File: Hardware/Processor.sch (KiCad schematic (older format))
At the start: 0 parts

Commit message: Add processor support circuitry
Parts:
- added C? (x2): C, ~, symbol C
- added C?: 10uF, ~, symbol C
- added C? (x2): 0.1uF, ~, symbol C
- added J?: ICSP-PIC, ~, symbol ICSP-PIC
- added J?: USB_MINI, ~, symbol USB_MINI
- added R? (x3): 10k, ~, symbol R
- added R?: R, ~, symbol R
- added SW?: PGM, ~, symbol SW-MOM
- added SW?: RST, ~, symbol SW-MOM
- added U?: PIC32MX250F128B, symbol PIC32MX250F128B
- added X?: 8MHz, ~, symbol CRYSTAL
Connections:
- net labels added: +3.3V, A1, A2, C, C1, C2, D+, D-, GND, ID, MCLR, OSC1, OSC2, PGC, PGD, PGM, VBus, VCap
- wire segments 0 -> 63
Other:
- note added: "A"

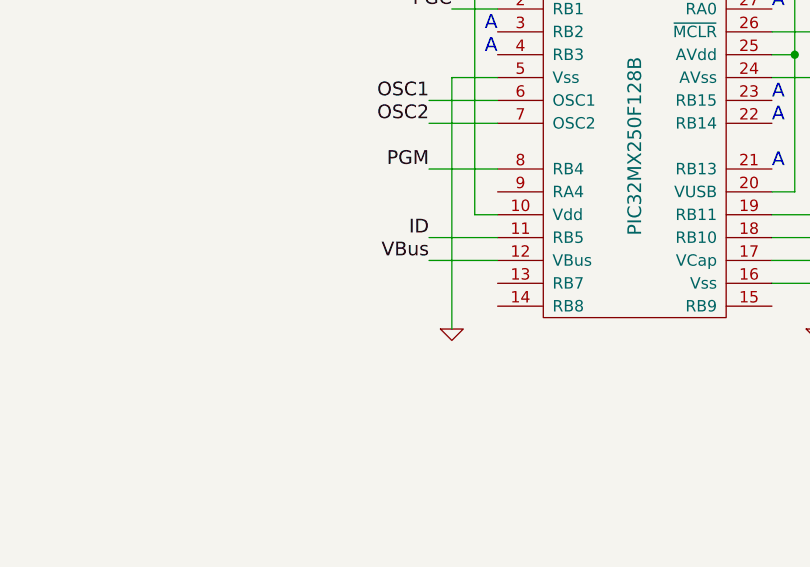
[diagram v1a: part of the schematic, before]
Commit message: Fill BOM fields of amplifier section
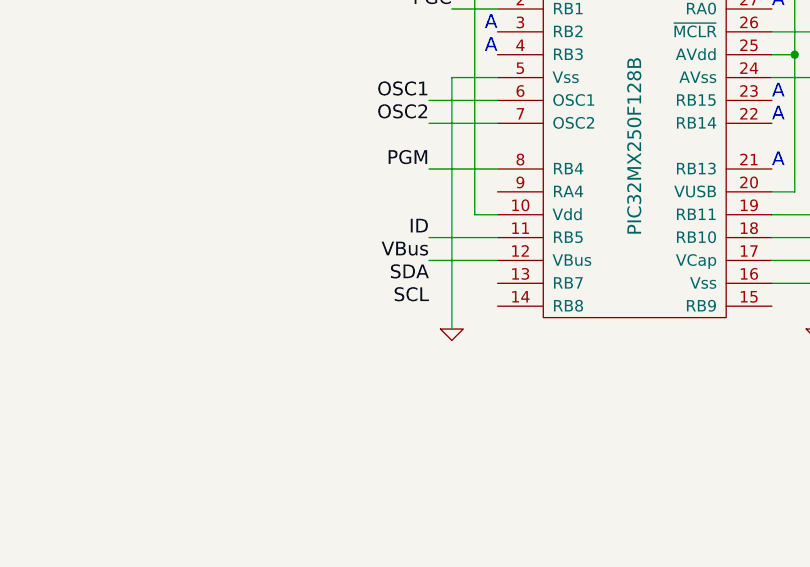
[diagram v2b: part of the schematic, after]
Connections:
- net labels added: SCL, SDA
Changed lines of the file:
@@
 Text Notes 5500 3700 2    60   ~ 0
 A
+Text Label 5200 4800 2    60   ~ 0
+SCL
+Text Label 5200 4700 2    60   ~ 0
+SDA
 $EndSCHEMATC

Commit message: Add second detection chain
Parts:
- removed C? (x2): 0.1uF, ~, symbol C
- removed R? (x2): 10k, ~, symbol R
- added C? (x2): 0.1uF, CAPC1608, symbol C
- added R? (x2): 10k, RESC1608, symbol R
- C?: footprint ~ -> CAPC2012; Dielectric D -> X5R; Distributor Part No (none) -> 1276-1052-1-ND; MFR Name (none) -> Samsung; MFR Part No (none) -> CL21A106KPFNNNE; Voltage V -> 10V
- R?: footprint ~ -> RESC1608; Distributor Part No (none) -> RMCF0603JT10K0CT-ND; MFR Name (none) -> Stackpole; MFR Part No (none) -> RMCF0603JT10K0; Power W -> 0.1W; Tolerance % -> 5%
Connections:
- wire segments 63 -> 72
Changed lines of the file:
@@
 $Descr A4 11693 8268
 encoding utf-8
-Sheet 5 5
+Sheet 5 7
 Title "Solid State Cosmic Ray Detector"
 Date "24 sep 2013"
@@
 $EndComp
 $Comp
-L R R?
-U 1 1 5240FDBF
-P 2600 2250
-F 0 "R?" H 2600 2350 50  0000 C CNN
-F 1 "10k" H 2600 2250 50  0000 C CNN
-F 2 "~" H 2600 2250 60  0000 C CNN
-F 3 "~" H 2600 2250 60  0000 C CNN
-F 4 "W" H 2600 2150 50  0001 C CNN "Power"
-F 5 "%" H 2600 2050 50  0001 C CNN "Tolerance"
-	1    2600 2250
-	0    1    -1   0
-$EndComp
-$Comp
 L GND #PWR?
 U 1 1 5240FDF5
@@
 	1    0    0    -1
 $EndComp
-Text Label 2700 2600 0    60   ~ 0
+Text Label 2800 2600 0    60   ~ 0
 MCLR
-Text Label 2700 2900 0    60   ~ 0
+Text Label 2800 2900 0    60   ~ 0
 PGD
-Text Label 2700 3000 0    60   ~ 0
+Text Label 2800 3000 0    60   ~ 0
 PGC
 $Comp
@@
 F 0 "C?" H 2150 7000 60  0000 L CNN
 F 1 "10uF" H 2150 6700 60  0000 L CNN
-F 2 "~" H 2100 6850 60  0000 C CNN
+F 2 "CAPC2012" H 2100 6850 60  0001 C CNN
 F 3 "~" H 2100 6850 60  0000 C CNN
-F 4 "V" H 2050 6700 60  0001 R CNN "Voltage"
-F 5 "D" H 2050 7000 60  0001 R CNN "Dielectric"
+F 4 "Samsung" H 2100 6850 60  0001 C CNN "MFR Name"
+F 5 "CL21A106KPFNNNE" H 2100 6850 60  0001 C CNN "MFR Part No"
+F 6 "1276-1052-1-ND" H 2100 6850 60  0001 C CNN "Distributor Part No"
+F 7 "10V" H 2050 6700 60  0000 R CNN "Voltage"
+F 8 "X5R" H 2050 7000 60  0000 R CNN "Dielectric"
 	1    2100 6850
 	1    0    0    -1
@@
 $EndComp
 Wire Wire Line
-	2500 1800 2500 2700
+	2500 1800 2500 1900
+Wire Wire Line
+	2500 1900 2500 2700
 Wire Wire Line
 	2500 2700 2400 2700
@@
 	2400 2600 2700 2600
 Wire Wire Line
-	2600 2500 2600 2600
-Connection ~ 2600 2600
-Wire Wire Line
-	2600 2000 2600 1900
-Wire Wire Line
-	2600 1900 2500 1900
+	2700 2600 2800 2600
+Wire Wire Line
+	2700 2500 2700 2600
+Connection ~ 2700 2600
+Wire Wire Line
+	2700 2000 2700 1900
+Wire Wire Line
+	2700 1900 2500 1900
 Connection ~ 2500 1900
 Wire Wire Line
-	2400 2900 2700 2900
-Wire Wire Line
-	2400 3000 2700 3000
-Wire Wire Line
-	2800 5100 2800 5300
-Wire Wire Line
-	2100 5100 2100 5300
+	2400 2900 2800 2900
+Wire Wire Line
+	2400 3000 2800 3000
+Wire Wire Line
+	2800 5100 2800 5200
+Wire Wire Line
+	2800 5200 2800 5300
+Wire Wire Line
+	2100 5100 2100 5200
+Wire Wire Line
+	2100 5200 2100 5300
 Wire Wire Line
 	2200 5200 2100 5200
@@
 	7000 3600 6700 3600
 Wire Wire Line
-	6800 3300 6800 4300
+	6800 3300 6800 3700
+Wire Wire Line
+	6800 3700 6800 4300
 Wire Wire Line
 	6800 3700 6700 3700
 Wire Wire Line
-	6900 3800 6900 4900
+	6900 3800 6900 4700
+Wire Wire Line
+	6900 4700 6900 4900
 Wire Wire Line
 	6900 3800 6700 3800
@@
 	2400 4100 2400 4200
 $Comp
-L C C?
-U 1 1 524102A6
-P 2600 6850
-F 0 "C?" H 2650 7000 60  0000 L CNN
-F 1 "0.1uF" H 2650 6700 60  0000 L CNN
-F 2 "~" H 2600 6850 60  0000 C CNN
-F 3 "~" H 2600 6850 60  0000 C CNN
-F 4 "V" H 2550 6700 60  0001 R CNN "Voltage"
-F 5 "D" H 2550 7000 60  0001 R CNN "Dielectric"
-	1    2600 6850
-	1    0    0    -1
-$EndComp
-$Comp
 L +3.3V #PWR?
 U 1 1 524102C8
-P 2800 6400
-F 0 "#PWR?" H 2800 6360 30  0001 C CNN
-F 1 "+3.3V" H 2800 6510 30  0000 C CNN
-F 2 "" H 2800 6400 60  0000 C CNN
-F 3 "" H 2800 6400 60  0000 C CNN
-	1    2800 6400
-	1    0    0    -1
-$EndComp
-$Comp
-L C C?
-U 1 1 524102D7
-P 3000 6850
-F 0 "C?" H 3050 7000 60  0000 L CNN
-F 1 "0.1uF" H 3050 6700 60  0000 L CNN
-F 2 "~" H 3000 6850 60  0000 C CNN
-F 3 "~" H 3000 6850 60  0000 C CNN
-F 4 "V" H 2950 6700 60  0001 R CNN "Voltage"
-F 5 "D" H 2950 7000 60  0001 R CNN "Dielectric"
-	1    3000 6850
-	1    0    0    -1
-$EndComp
-Wire Wire Line
-	2600 6600 2600 6500
-Wire Wire Line
-	2600 6500 3000 6500
-Wire Wire Line
-	3000 6500 3000 6600
-Wire Wire Line
-	2600 7100 2600 7200
-Wire Wire Line
-	2600 7200 3000 7200
-Wire Wire Line
-	3000 7200 3000 7100
+P 3000 6400
+F 0 "#PWR?" H 3000 6360 30  0001 C CNN
+F 1 "+3.3V" H 3000 6510 30  0000 C CNN
+F 2 "" H 3000 6400 60  0000 C CNN
+F 3 "" H 3000 6400 60  0000 C CNN
+	1    3000 6400
+	1    0    0    -1
+$EndComp
+Wire Wire Line
+	2700 6600 2700 6500
+Wire Wire Line
+	2700 6500 3000 6500
+Wire Wire Line
+	3000 6500 3300 6500
+Wire Wire Line
+	2700 7100 2700 7200
+Wire Wire Line
+	2700 7200 3000 7200
+Wire Wire Line
+	3000 7200 3300 7200
 $Comp
 L GND #PWR?
 U 1 1 5241033E
-P 2800 7300
-F 0 "#PWR?" H 2800 7300 30  0001 C CNN
-F 1 "GND" H 2800 7230 30  0001 C CNN
-F 2 "" H 2800 7300 60  0000 C CNN
-F 3 "" H 2800 7300 60  0000 C CNN
-	1    2800 7300
-	1    0    0    -1
-$EndComp
-Wire Wire Line
-	2800 7300 2800 7200
-Connection ~ 2800 7200
-Wire Wire Line
-	2800 6400 2800 6500
-Connection ~ 2800 6500
+P 3000 7300
+F 0 "#PWR?" H 3000 7300 30  0001 C CNN
+F 1 "GND" H 3000 7230 30  0001 C CNN
+F 2 "" H 3000 7300 60  0000 C CNN
+F 3 "" H 3000 7300 60  0000 C CNN
+	1    3000 7300
+	1    0    0    -1
+$EndComp
+Wire Wire Line
+	3000 7200 3000 7300
+Connection ~ 3000 7200
+Wire Wire Line
+	3000 6500 3000 6400
+Connection ~ 3000 6500
 Text Label 5300 3400 2    60   ~ 0
 PGD
@@
 F 0 "R?" H 5050 1400 50  0000 C CNN
 F 1 "10k" H 5050 1300 50  0000 C CNN
-F 2 "~" H 5050 1300 60  0000 C CNN
+F 2 "RESC1608" H 5050 1300 60  0001 C CNN
 F 3 "~" H 5050 1300 60  0000 C CNN
-F 4 "W" H 5050 1200 50  0001 C CNN "Power"
-F 5 "%" H 5050 1100 50  0001 C CNN "Tolerance"
+F 4 "Stackpole" H 5050 1300 60  0001 C CNN "MFR Name"
+F 5 "RMCF0603JT10K0" H 5050 1300 60  0001 C CNN "MFR Part No"
+F 6 "RMCF0603JT10K0CT-ND" H 5050 1300 60  0001 C CNN "Distributor Part No"
+F 7 "0.1W" H 5050 1200 50  0000 C CNN "Power"
+F 8 "5%" H 5050 1100 50  0001 C CNN "Tolerance"
 	1    5050 1300
 	1    0    0    -1
-$EndComp
-$Comp
-L R R?
-U 1 1 5241047B
-P 5400 1650
-F 0 "R?" H 5400 1750 50  0000 C CNN
-F 1 "10k" H 5400 1650 50  0000 C CNN
-F 2 "~" H 5400 1650 60  0000 C CNN
-F 3 "~" H 5400 1650 60  0000 C CNN
-F 4 "W" H 5400 1550 50  0001 C CNN "Power"
-F 5 "%" H 5400 1450 50  0001 C CNN "Tolerance"
-	1    5400 1650
-	0    -1   -1   0
 $EndComp
 $Comp
@@
 	4700 1300 4800 1300
 Wire Wire Line
-	5300 1300 5500 1300
+	5300 1300 5400 1300
+Wire Wire Line
+	5400 1300 5500 1300
 $Comp
 L GND #PWR?
@@
 Text Label 5200 4700 2    60   ~ 0
 SDA
+$Comp
+L C C?
+U 1 1 52414536
+P 3300 6850
+F 0 "C?" H 3350 7000 60  0000 L CNN
+F 1 "0.1uF" H 3350 6700 60  0000 L CNN
+F 2 "CAPC1608" H 3300 6850 60  0001 C CNN
+F 3 "~" H 3300 6850 60  0000 C CNN
+F 4 "Samsung" H 3300 6850 60  0001 C CNN "MFR Name"
+F 5 "CL10B104KO8NNNC" H 3300 6850 60  0001 C CNN "MFR Part No"
+F 6 "1276-1005-1-ND" H 3300 6850 60  0001 C CNN "Distributor Part No"
+F 7 "16V" H 3250 6700 60  0000 R CNN "Voltage"
+F 8 "X7R" H 3250 7000 60  0000 R CNN "Dielectric"
+	1    3300 6850
+	1    0    0    -1
+$EndComp
+$Comp
+L C C?
+U 1 1 52414541
+P 2700 6850
+F 0 "C?" H 2750 7000 60  0000 L CNN
+F 1 "0.1uF" H 2750 6700 60  0000 L CNN
+F 2 "CAPC1608" H 2700 6850 60  0001 C CNN
+F 3 "~" H 2700 6850 60  0000 C CNN
+F 4 "Samsung" H 2700 6850 60  0001 C CNN "MFR Name"
+F 5 "CL10B104KO8NNNC" H 2700 6850 60  0001 C CNN "MFR Part No"
+F 6 "1276-1005-1-ND" H 2700 6850 60  0001 C CNN "Distributor Part No"
+F 7 "16V" H 2650 6700 60  0000 R CNN "Voltage"
+F 8 "X7R" H 2650 7000 60  0000 R CNN "Dielectric"
+	1    2700 6850
+	1    0    0    -1
+$EndComp
+Wire Wire Line
+	3300 7200 3300 7100
+Wire Wire Line
+	3300 6500 3300 6600
+$Comp
+L R R?
+U 1 1 5241462B
+P 5400 1650
+F 0 "R?" H 5400 1750 50  0000 C CNN
+F 1 "10k" H 5400 1650 50  0000 C CNN
+F 2 "RESC1608" H 5400 1650 60  0001 C CNN
+F 3 "~" H 5400 1650 60  0000 C CNN
+F 4 "Stackpole" H 5400 1650 60  0001 C CNN "MFR Name"
+F 5 "RMCF0603JT10K0" H 5400 1650 60  0001 C CNN "MFR Part No"
+F 6 "RMCF0603JT10K0CT-ND" H 5400 1650 60  0001 C CNN "Distributor Part No"
+F 7 "0.1W" H 5400 1550 50  0000 C CNN "Power"
+F 8 "5%" H 5400 1450 50  0001 C CNN "Tolerance"
+	1    5400 1650
+	0    -1   -1   0
+$EndComp
+$Comp
+L R R?
+U 1 1 52414636
+P 2700 2250
+F 0 "R?" H 2700 2350 50  0000 C CNN
+F 1 "10k" H 2700 2250 50  0000 C CNN
+F 2 "RESC1608" H 2700 2250 60  0001 C CNN
+F 3 "~" H 2700 2250 60  0000 C CNN
+F 4 "Stackpole" H 2700 2250 60  0001 C CNN "MFR Name"
+F 5 "RMCF0603JT10K0" H 2700 2250 60  0001 C CNN "MFR Part No"
+F 6 "RMCF0603JT10K0CT-ND" H 2700 2250 60  0001 C CNN "Distributor Part No"
+F 7 "0.1W" H 2700 2150 50  0000 C CNN "Power"
+F 8 "5%" H 2700 2050 50  0001 C CNN "Tolerance"
+	1    2700 2250
+	0    1    1    0
+$EndComp
 $EndSCHEMATC

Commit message: Initial annotation
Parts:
- gave numbers to parts that had none: 15
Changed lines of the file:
@@
 $EndDescr
 $Comp
-L PIC32MX250F128B U?
+L PIC32MX250F128B U5
 U 1 1 5240FCEE
 P 6100 4100
-F 0 "U?" H 6100 4900 60  0000 C CNN
+F 0 "U5" H 6100 4900 60  0000 C CNN
 F 1 "PIC32MX250F128B" V 6100 4100 60  0000 C CNN
 F 2 "" H 6100 4100 60  0000 C CNN
@@
 $EndComp
 $Comp
-L ICSP-PIC J?
+L ICSP-PIC J1
 U 1 1 5240FD97
 P 2050 2800
-F 0 "J?" H 2050 3100 60  0000 C CNN
+F 0 "J1" H 2050 3100 60  0000 C CNN
 F 1 "ICSP-PIC" V 1850 2800 60  0000 C CNN
 F 2 "~" H 2050 3100 60  0000 C CNN
@@
 $EndComp
 $Comp
-L +3.3V #PWR?
+L +3.3V #PWR32
 U 1 1 5240FDA6
 P 2500 1800
-F 0 "#PWR?" H 2500 1760 30  0001 C CNN
+F 0 "#PWR32" H 2500 1760 30  0001 C CNN
 F 1 "+3.3V" H 2500 1910 30  0000 C CNN
 F 2 "" H 2500 1800 60  0000 C CNN
@@
 $EndComp
 $Comp
-L GND #PWR?
+L GND #PWR35
 U 1 1 5240FDF5
 P 2500 3100
-F 0 "#PWR?" H 2500 3100 30  0001 C CNN
+F 0 "#PWR35" H 2500 3100 30  0001 C CNN
 F 1 "GND" H 2500 3030 30  0001 C CNN
 F 2 "" H 2500 3100 60  0000 C CNN
@@
 PGC
 $Comp
-L CRYSTAL X?
+L CRYSTAL X1
 U 1 1 5240FEA6
 P 2450 5200
-F 0 "X?" H 2450 5350 60  0000 C CNN
+F 0 "X1" H 2450 5350 60  0000 C CNN
 F 1 "8MHz" H 2450 5050 60  0000 C CNN
 F 2 "~" H 2450 5200 60  0000 C CNN
@@
 $EndComp
 $Comp
-L C C?
+L C C17
 U 1 1 5240FEB5
 P 2800 5550
-F 0 "C?" H 2850 5700 60  0000 L CNN
+F 0 "C17" H 2850 5700 60  0000 L CNN
 F 1 "C" H 2850 5400 60  0000 L CNN
 F 2 "~" H 2800 5550 60  0000 C CNN
@@
 $EndComp
 $Comp
-L C C?
+L C C16
 U 1 1 5240FED5
 P 2100 5550
-F 0 "C?" H 2150 5700 60  0000 L CNN
+F 0 "C16" H 2150 5700 60  0000 L CNN
 F 1 "C" H 2150 5400 60  0000 L CNN
 F 2 "~" H 2100 5550 60  0000 C CNN
@@
 OSC2
 $Comp
-L GND #PWR?
+L GND #PWR41
 U 1 1 5240FF54
 P 2100 5900
-F 0 "#PWR?" H 2100 5900 30  0001 C CNN
+F 0 "#PWR41" H 2100 5900 30  0001 C CNN
 F 1 "GND" H 2100 5830 30  0001 C CNN
 F 2 "" H 2100 5900 60  0000 C CNN
@@
 $EndComp
 $Comp
-L GND #PWR?
+L GND #PWR42
 U 1 1 5240FF63
 P 2800 5900
-F 0 "#PWR?" H 2800 5900 30  0001 C CNN
+F 0 "#PWR42" H 2800 5900 30  0001 C CNN
 F 1 "GND" H 2800 5830 30  0001 C CNN
 F 2 "" H 2800 5900 60  0000 C CNN
@@
 OSC2
 $Comp
-L USB_MINI J?
+L USB_MINI J2
 U 1 1 5240FF9C
 P 2000 3850
-F 0 "J?" H 2000 4150 60  0000 C CNN
+F 0 "J2" H 2000 4150 60  0000 C CNN
 F 1 "USB_MINI" H 2000 3450 60  0000 C CNN
 F 2 "~" H 2000 3850 60  0000 C CNN
@@
 MCLR
 $Comp
-L C C?
+L C C18
 U 1 1 5240FFDF
 P 2100 6850
-F 0 "C?" H 2150 7000 60  0000 L CNN
+F 0 "C18" H 2150 7000 60  0000 L CNN
 F 1 "10uF" H 2150 6700 60  0000 L CNN
 F 2 "CAPC2012" H 2100 6850 60  0001 C CNN
@@
 $EndComp
 $Comp
-L +3.3V #PWR?
+L +3.3V #PWR37
 U 1 1 5240FFFE
 P 6800 3300
-F 0 "#PWR?" H 6800 3260 30  0001 C CNN
+F 0 "#PWR37" H 6800 3260 30  0001 C CNN
 F 1 "+3.3V" H 6800 3410 30  0000 C CNN
 F 2 "" H 6800 3300 60  0000 C CNN
@@
 $EndComp
 $Comp
-L GND #PWR?
+L GND #PWR40
 U 1 1 52410043
 P 6900 4900
-F 0 "#PWR?" H 6900 4900 30  0001 C CNN
+F 0 "#PWR40" H 6900 4900 30  0001 C CNN
 F 1 "GND" H 6900 4830 30  0001 C CNN
 F 2 "" H 6900 4900 60  0000 C CNN
@@
 $EndComp
 $Comp
-L +3.3V #PWR?
+L +3.3V #PWR36
 U 1 1 524100A6
 P 5400 3300
-F 0 "#PWR?" H 5400 3260 30  0001 C CNN
+F 0 "#PWR36" H 5400 3260 30  0001 C CNN
 F 1 "+3.3V" H 5400 3410 30  0000 C CNN
 F 2 "" H 5400 3300 60  0000 C CNN
@@
 $EndComp
 $Comp
-L GND #PWR?
+L GND #PWR39
 U 1 1 524100D5
 P 5300 4900
-F 0 "#PWR?" H 5300 4900 30  0001 C CNN
+F 0 "#PWR39" H 5300 4900 30  0001 C CNN
 F 1 "GND" H 5300 4830 30  0001 C CNN
 F 2 "" H 5300 4900 60  0000 C CNN
@@
 $EndComp
 $Comp
-L GND #PWR?
+L GND #PWR44
 U 1 1 5241010B
 P 2100 7200
-F 0 "#PWR?" H 2100 7200 30  0001 C CNN
+F 0 "#PWR44" H 2100 7200 30  0001 C CNN
 F 1 "GND" H 2100 7130 30  0001 C CNN
 F 2 "" H 2100 7200 60  0000 C CNN
@@
 	2100 6500 2100 6600
 $Comp
-L GND #PWR?
+L GND #PWR38
 U 1 1 524101F5
 P 2400 4200
-F 0 "#PWR?" H 2400 4200 30  0001 C CNN
+F 0 "#PWR38" H 2400 4200 30  0001 C CNN
 F 1 "GND" H 2400 4130 30  0001 C CNN
 F 2 "" H 2400 4200 60  0000 C CNN
@@
 	2400 4100 2400 4200
 $Comp
-L +3.3V #PWR?
+L +3.3V #PWR43
 U 1 1 524102C8
 P 3000 6400
-F 0 "#PWR?" H 3000 6360 30  0001 C CNN
+F 0 "#PWR43" H 3000 6360 30  0001 C CNN
 F 1 "+3.3V" H 3000 6510 30  0000 C CNN
 F 2 "" H 3000 6400 60  0000 C CNN
@@
 	3000 7200 3300 7200
 $Comp
-L GND #PWR?
+L GND #PWR45
 U 1 1 5241033E
 P 3000 7300
-F 0 "#PWR?" H 3000 7300 30  0001 C CNN
+F 0 "#PWR45" H 3000 7300 30  0001 C CNN
 F 1 "GND" H 3000 7230 30  0001 C CNN
 F 2 "" H 3000 7300 60  0000 C CNN
@@
 PGM
 $Comp
-L R R?
+L R R12
 U 1 1 52410460
 P 5050 1300
-F 0 "R?" H 5050 1400 50  0000 C CNN
+F 0 "R12" H 5050 1400 50  0000 C CNN
 F 1 "10k" H 5050 1300 50  0000 C CNN
 F 2 "RESC1608" H 5050 1300 60  0001 C CNN
@@
 $EndComp
 $Comp
-L SW-MOM SW?
+L SW-MOM SW1
 U 1 1 52410496
 P 5750 1300
-F 0 "SW?" H 5750 1450 60  0000 C CNN
+F 0 "SW1" H 5750 1450 60  0000 C CNN
 F 1 "PGM" H 5750 1200 60  0000 C CNN
 F 2 "~" H 5750 1300 60  0000 C CNN
@@
 	5400 1300 5500 1300
 $Comp
-L GND #PWR?
+L GND #PWR33
 U 1 1 5241051A
 P 5400 2000
-F 0 "#PWR?" H 5400 2000 30  0001 C CNN
+F 0 "#PWR33" H 5400 2000 30  0001 C CNN
 F 1 "GND" H 5400 1930 30  0001 C CNN
 F 2 "" H 5400 2000 60  0000 C CNN
@@
 $EndComp
 $Comp
-L +3.3V #PWR?
+L +3.3V #PWR31
 U 1 1 52410529
 P 6100 1200
-F 0 "#PWR?" H 6100 1160 30  0001 C CNN
+F 0 "#PWR31" H 6100 1160 30  0001 C CNN
 F 1 "+3.3V" H 6100 1310 30  0000 C CNN
 F 2 "" H 6100 1200 60  0000 C CNN
@@
 	5400 1900 5400 2000
 $Comp
-L SW-MOM SW?
+L SW-MOM SW2
 U 1 1 52410607
 P 5750 2300
-F 0 "SW?" H 5750 2450 60  0000 C CNN
+F 0 "SW2" H 5750 2450 60  0000 C CNN
 F 1 "RST" H 5750 2200 60  0000 C CNN
 F 2 "~" H 5750 2300 60  0000 C CNN
@@
 $EndComp
 $Comp
-L GND #PWR?
+L GND #PWR34
 U 1 1 52410620
 P 6100 2400
-F 0 "#PWR?" H 6100 2400 30  0001 C CNN
+F 0 "#PWR34" H 6100 2400 30  0001 C CNN
 F 1 "GND" H 6100 2330 30  0001 C CNN
 F 2 "" H 6100 2400 60  0000 C CNN
@@
 	6100 2300 6000 2300
 $Comp
-L R R?
+L R R15
 U 1 1 52410670
 P 5050 2300
-F 0 "R?" H 5050 2400 50  0000 C CNN
+F 0 "R15" H 5050 2400 50  0000 C CNN
 F 1 "R" H 5050 2300 50  0000 C CNN
 F 2 "~" H 5050 2300 60  0000 C CNN
@@
 SDA
 $Comp
-L C C?
+L C C20
 U 1 1 52414536
 P 3300 6850
-F 0 "C?" H 3350 7000 60  0000 L CNN
+F 0 "C20" H 3350 7000 60  0000 L CNN
 F 1 "0.1uF" H 3350 6700 60  0000 L CNN
 F 2 "CAPC1608" H 3300 6850 60  0001 C CNN
@@
 $EndComp
 $Comp
-L C C?
+L C C19
 U 1 1 52414541
 P 2700 6850
-F 0 "C?" H 2750 7000 60  0000 L CNN
+F 0 "C19" H 2750 7000 60  0000 L CNN
 F 1 "0.1uF" H 2750 6700 60  0000 L CNN
 F 2 "CAPC1608" H 2700 6850 60  0001 C CNN
@@
 	3300 6500 3300 6600
 $Comp
-L R R?
+L R R13
 U 1 1 5241462B
 P 5400 1650
-F 0 "R?" H 5400 1750 50  0000 C CNN
+F 0 "R13" H 5400 1750 50  0000 C CNN
 F 1 "10k" H 5400 1650 50  0000 C CNN
 F 2 "RESC1608" H 5400 1650 60  0001 C CNN
@@
 $EndComp
 $Comp
-L R R?
+L R R14
 U 1 1 52414636
 P 2700 2250
-F 0 "R?" H 2700 2350 50  0000 C CNN
+F 0 "R14" H 2700 2350 50  0000 C CNN
 F 1 "10k" H 2700 2250 50  0000 C CNN
 F 2 "RESC1608" H 2700 2250 60  0001 C CNN
